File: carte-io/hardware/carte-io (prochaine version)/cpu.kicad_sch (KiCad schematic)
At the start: 24 parts, among them J3 FTSH-105-01-L-DV-007, SW1 SW_Push, SW2 SW_Push, U1 STM32U545VETx, X1 ASE-16.000MHZ-LC-T

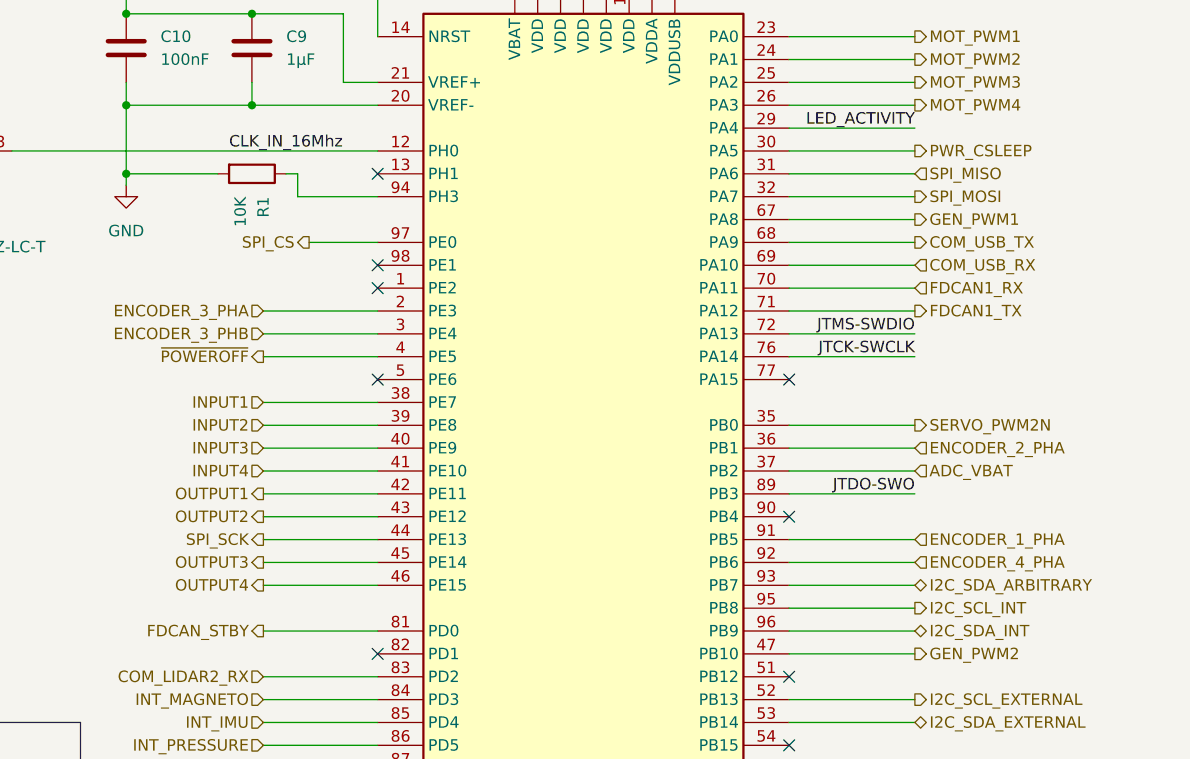
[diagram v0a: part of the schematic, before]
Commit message: Commit de sauvegarde, gros changement sur la carte IO, les connecteurs sont compatibles SeeedStudio Grove. Il faut reprendre une grosse partie du routage et rajouter deux entrées analogiques
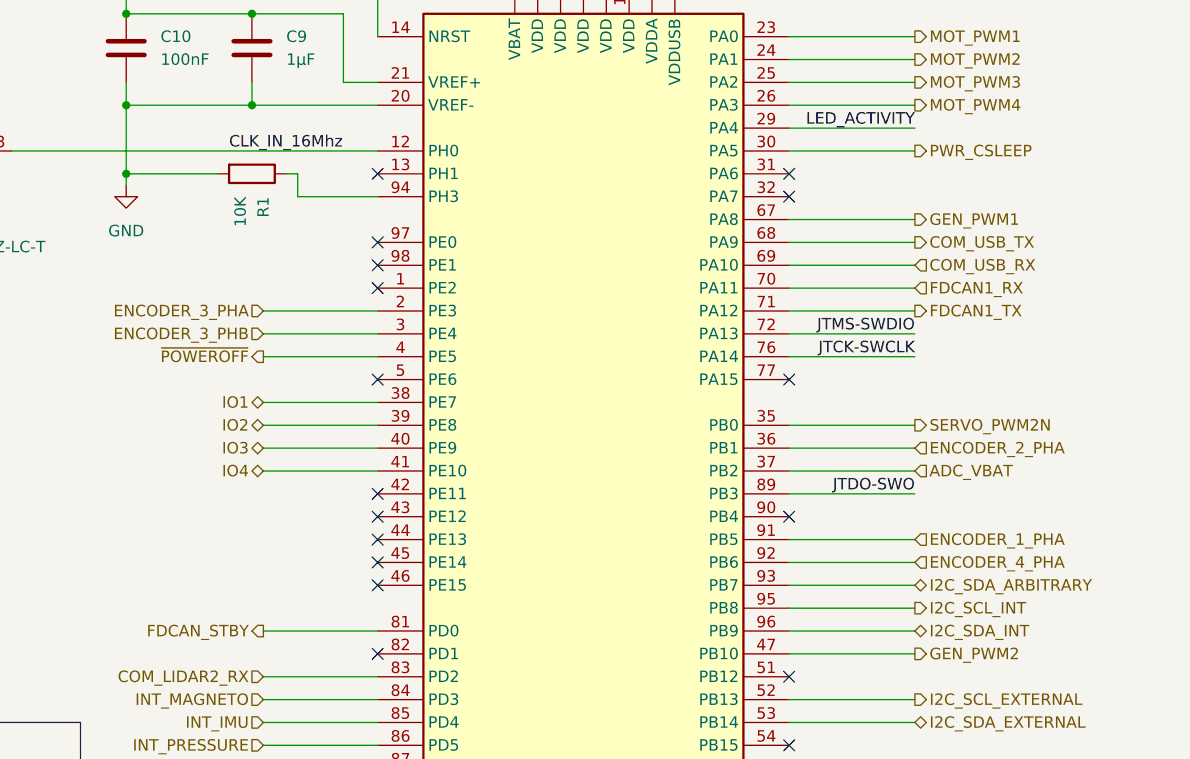
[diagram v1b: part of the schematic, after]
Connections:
- net INPUT1 renamed IO1
- net INPUT2 renamed IO2
- net INPUT3 renamed IO3
- net INPUT4 renamed IO4
- net OUTPUT1: no longer names the net of U1.42 (PE11)
- net OUTPUT2: no longer names the net of U1.43 (PE12)
- net OUTPUT3: no longer names the net of U1.45 (PE14)
- net OUTPUT4: no longer names the net of U1.46 (PE15)
- net SPI_CS: no longer names the net of U1.97 (PE0)
- net SPI_MISO: no longer names the net of U1.31 (PA6)
- net SPI_MOSI: no longer names the net of U1.32 (PA7)
- net SPI_SCK: no longer names the net of U1.44 (PE13)
- no-connect marks 18 -> 26
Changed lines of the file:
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@@
+	)
+	(no_connect
+		(at 104.14 58.42)
+	)
+	(no_connect
+		(at 104.14 86.36)
 	)
 	(no_connect
@@
 	)
 	(no_connect
+		(at 149.86 53.34)
+	)
+	(no_connect
+		(at 104.14 88.9)
+	)
+	(no_connect
+		(at 104.14 91.44)
+	)
+	(no_connect
 		(at 149.86 154.94)
 	)
@@
 	)
 	(no_connect
+		(at 149.86 50.8)
+	)
+	(no_connect
 		(at 104.14 60.96)
 	)
@@
 	)
 	(no_connect
+		(at 104.14 96.52)
+	)
+	(no_connect
 		(at 149.86 157.48)
 	)
@@
 	)
 	(no_connect
+		(at 104.14 93.98)
+	)
+	(no_connect
 		(at 104.14 137.16)
 	)
@@
 	(wire
 		(pts
-			(xy 91.44 91.44) (xy 104.14 91.44)
-		)
-		(stroke
-			(width 0)
-			(type default)
-		)
-	)
-	(wire
-		(pts
 			(xy 50.8 187.96) (xy 58.42 187.96)
 		)
@@
 	(wire
 		(pts
-			(xy 91.44 86.36) (xy 104.14 86.36)
-		)
-		(stroke
-			(width 0)
-			(type default)
-		)
-	)
-	(wire
-		(pts
 			(xy 58.42 187.96) (xy 58.42 189.23)
 		)
@@
 	(wire
 		(pts
-			(xy 91.44 93.98) (xy 104.14 93.98)
-		)
-		(stroke
-			(width 0)
-			(type default)
-		)
-	)
-	(wire
-		(pts
 			(xy 149.86 109.22) (xy 163.83 109.22)
 		)
@@
 	(wire
 		(pts
-			(xy 91.44 88.9) (xy 104.14 88.9)
-		)
-		(stroke
-			(width 0)
-			(type default)
-		)
-	)
-	(wire
-		(pts
 			(xy 25.4 130.81) (xy 25.4 128.27)
 		)
@@
 	(wire
 		(pts
-			(xy 149.86 50.8) (xy 163.83 50.8)
-		)
-		(stroke
-			(width 0)
-			(type default)
-		)
-	)
-	(wire
-		(pts
-			(xy 91.44 96.52) (xy 104.14 96.52)
-		)
-		(stroke
-			(width 0)
-			(type default)
-		)
-	)
-	(wire
-		(pts
 			(xy 76.2 43.18) (xy 90.17 43.18)
 		)
@@
 	(wire
 		(pts
-			(xy 96.52 58.42) (xy 104.14 58.42)
-		)
-		(stroke
-			(width 0)
-			(type default)
-		)
-	)
-	(wire
-		(pts
 			(xy 149.86 71.12) (xy 163.83 71.12)
 		)
@@
 		(pts
 			(xy 127 25.4) (xy 129.54 25.4)
-		)
-		(stroke
-			(width 0)
-			(type default)
-		)
-	)
-	(wire
-		(pts
-			(xy 149.86 53.34) (xy 163.83 53.34)
 		)
 		(stroke
@@
 		)
 	)
-	(hierarchical_label "OUTPUT2"
-		(shape output)
-		(at 91.44 88.9 180)
-		(effects
-			(font
-				(size 1.27 1.27)
-			)
-			(justify right)
-		)
-	)
 	(hierarchical_label "GEN_PWM1"
 		(shape output)
@@
 		)
 	)
-	(hierarchical_label "OUTPUT3"
-		(shape output)
-		(at 91.44 93.98 180)
-		(effects
-			(font
-				(size 1.27 1.27)
-			)
-			(justify right)
-		)
-	)
 	(hierarchical_label "COM_USB_RX"
 		(shape input)
@@
 		)
 	)
-	(hierarchical_label "SPI_SCK"
-		(shape output)
-		(at 91.44 91.44 180)
-		(effects
-			(font
-				(size 1.27 1.27)
-			)
-			(justify right)
-		)
-	)
-	(hierarchical_label "SPI_MOSI"
-		(shape output)
-		(at 163.83 53.34 0)
-		(effects
-			(font
-				(size 1.27 1.27)
-			)
-			(justify left)
-		)
-	)
-	(hierarchical_label "OUTPUT1"
-		(shape output)
-		(at 91.44 86.36 180)
-		(effects
-			(font
-				(size 1.27 1.27)
-			)
-			(justify right)
-		)
-	)
 	(hierarchical_label "GEN_PWM2"
 		(shape output)
@@
 		)
 	)
-	(hierarchical_label "INPUT3"
-		(shape input)
+	(hierarchical_label "IO3"
+		(shape bidirectional)
 		(at 91.44 81.28 180)
 		(effects
@@
 		)
 	)
-	(hierarchical_label "OUTPUT4"
-		(shape output)
-		(at 91.44 96.52 180)
-		(effects
-			(font
-				(size 1.27 1.27)
-			)
-			(justify right)
-		)
-	)
 	(hierarchical_label "ENCODER_2_PHB"
 		(shape input)
@@
 		)
 	)
-	(hierarchical_label "INPUT4"
-		(shape input)
+	(hierarchical_label "IO4"
+		(shape bidirectional)
 		(at 91.44 83.82 180)
 		(effects
@@
 		)
 	)
-	(hierarchical_label "INPUT2"
-		(shape input)
+	(hierarchical_label "IO2"
+		(shape bidirectional)
 		(at 91.44 78.74 180)
 		(effects
@@
 		)
 	)
-	(hierarchical_label "SPI_CS"
-		(shape output)
-		(at 96.52 58.42 180)
-		(effects
-			(font
-				(size 1.27 1.27)
-			)
-			(justify right)
-		)
-	)
 	(hierarchical_label "ADC_VBAT"
 		(shape input)
@@
 		)
 	)
-	(hierarchical_label "INPUT1"
-		(shape input)
+	(hierarchical_label "IO1"
+		(shape bidirectional)
 		(at 91.44 76.2 180)
 		(effects
@@
 		(effects
 			(font
-				(size 1.27 1.27)
-			)
-			(justify left)
-		)
-	)
-	(hierarchical_label "SPI_MISO"
-		(shape input)
-		(at 163.83 50.8 0)
-		(effects
-			(font

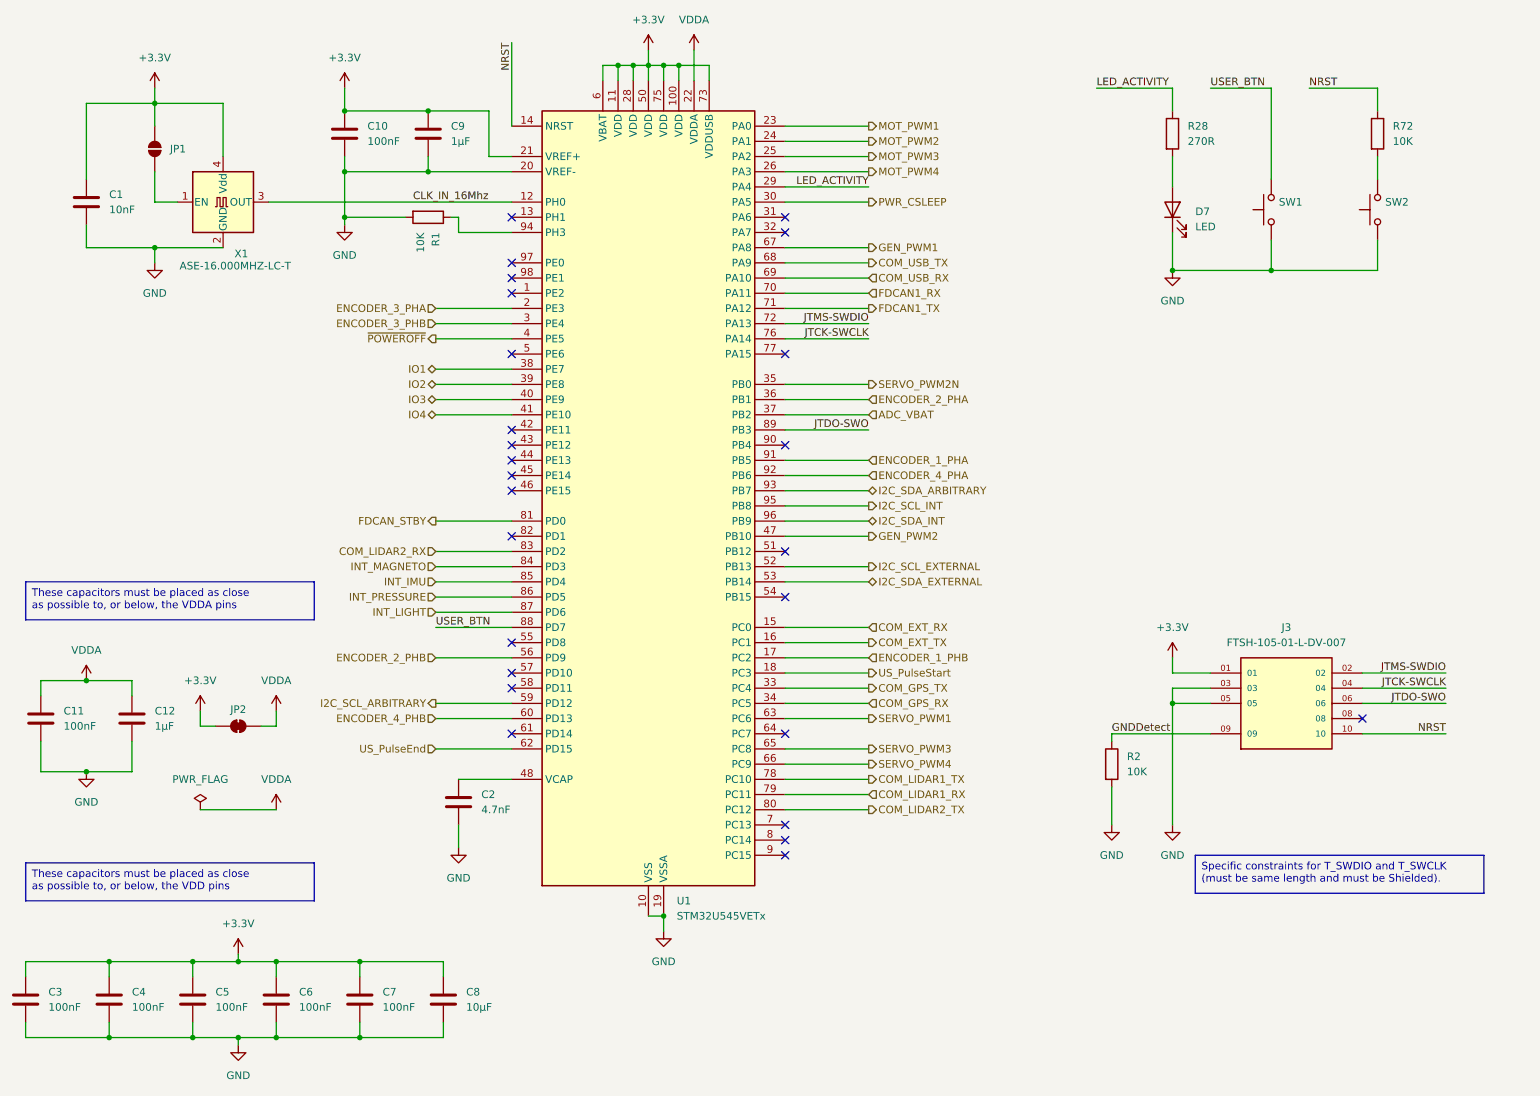
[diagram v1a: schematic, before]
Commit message: -- reorganisation de la carte, - rajout des connecteurs seeedstudio grove - Rajout des deux entrées ADC
travail en cours
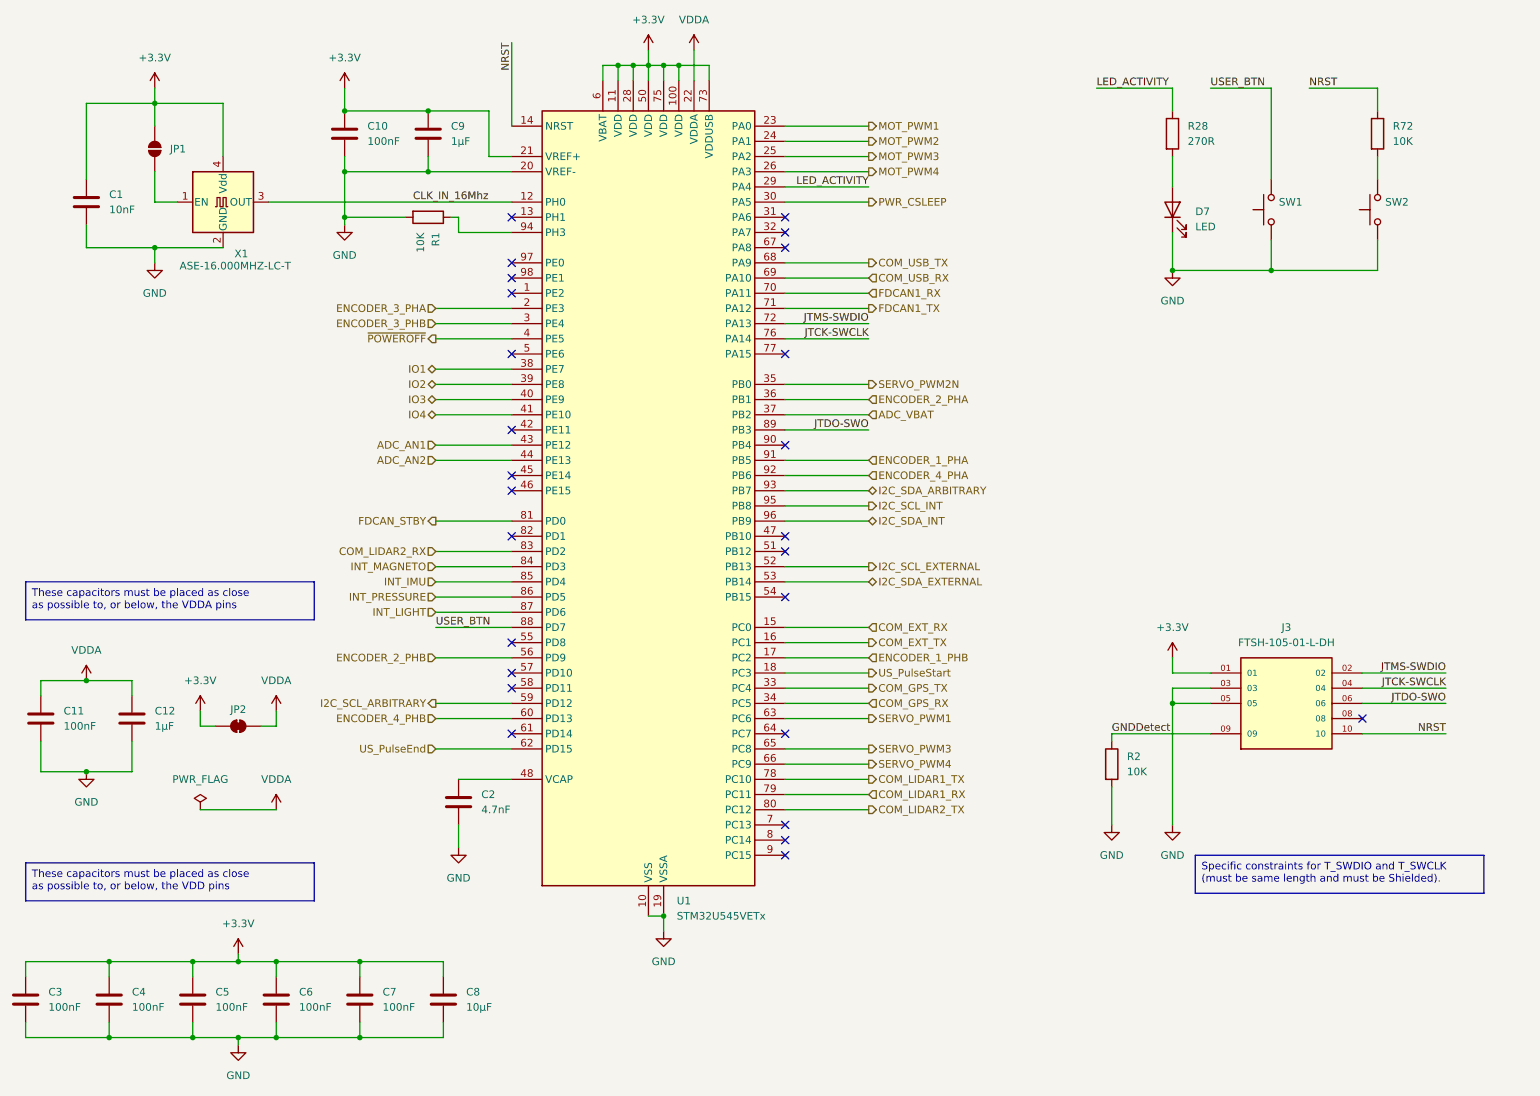
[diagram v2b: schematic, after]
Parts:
- J3: value FTSH-105-01-L-DV-007 -> FTSH-105-01-L-DH; footprint FTSH-105-01-L-DV-007-K:SAMTEC_FTSH-105-X-X-DV-007-P-X -> FTSH-105-01-L-DH:SAMTEC_FTSH-105-01-L-DH
- SW1, SW2: footprint Button_Switch_THT:SW_TH_Tactile_Omron_B3F-10xx -> Button_Switch_SMD:Panasonic_EVQPUJ_EVQPUA
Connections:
- net ADC_AN1: now reaches U1.43 (PE12)
- net ADC_AN2: now reaches U1.44 (PE13)
- net GEN_PWM1: no longer names the net of U1.67 (PA8)
- net GEN_PWM2: no longer names the net of U1.47 (PB10)
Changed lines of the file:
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@@
 	)
 	(no_connect
+		(at 149.86 104.14)
+	)
+	(no_connect
 		(at 104.14 86.36)
 	)
@@
 	)
 	(no_connect
-		(at 104.14 88.9)
-	)
-	(no_connect
-		(at 104.14 91.44)
-	)
-	(no_connect
 		(at 149.86 154.94)
 	)
@@
 	)
 	(no_connect
+		(at 149.86 55.88)
+	)
+	(no_connect
 		(at 149.86 73.66)
 	)
@@
 	(wire
 		(pts
+			(xy 91.44 88.9) (xy 104.14 88.9)
+		)
+		(stroke
+			(width 0)
+			(type default)
+		)
+	)
+	(wire
+		(pts
 			(xy 129.54 25.4) (xy 129.54 27.94)
 		)
@@
 	(wire
 		(pts
-			(xy 149.86 104.14) (xy 163.83 104.14)
-		)
-		(stroke
-			(width 0)
-			(type default)
-		)
-	)
-	(wire
-		(pts
 			(xy 91.44 124.46) (xy 104.14 124.46)
 		)
@@
 	(wire
 		(pts
+			(xy 91.44 91.44) (xy 104.14 91.44)
+		)
+		(stroke
+			(width 0)
+			(type default)
+		)
+	)
+	(wire
+		(pts
 			(xy 149.86 109.22) (xy 163.83 109.22)
 		)
@@
 	(wire
 		(pts
-			(xy 149.86 55.88) (xy 163.83 55.88)
-		)
-		(stroke
-			(width 0)
-			(type default)
-		)
-	)
-	(wire
-		(pts
 			(xy 44.45 55.88) (xy 44.45 58.42)
 		)
@@
 		)
 	)
-	(hierarchical_label "GEN_PWM1"
-		(shape output)
-		(at 163.83 55.88 0)
-		(effects
-			(font
-				(size 1.27 1.27)
-			)
-			(justify left)
-		)
-	)
 	(hierarchical_label "US_PulseStart"
 		(shape output)
@@
 		)
 	)
-	(hierarchical_label "GEN_PWM2"
-		(shape output)
-		(at 163.83 104.14 0)
+	(hierarchical_label "ADC_AN1"
+		(shape input)
+		(at 91.44 88.9 180)
 		(effects
 			(font
 				(size 1.27 1.27)
 			)
-			(justify left)
+			(justify right)
 		)
 	)
@@
 		)
 	)
+	(hierarchical_label "ADC_AN2"
+		(shape input)
+		(at 91.44 91.44 180)
+		(effects
+			(font
+				(size 1.27 1.27)
+			)
+			(justify right)
+		)
+	)
 	(hierarchical_label "COM_USB_TX"
 		(shape output)
@@
 			)
 		)
-		(property "Footprint" "Button_Switch_THT:SW_TH_Tactile_Omron_B3F-10xx"
+		(property "Footprint" "Button_Switch_SMD:Panasonic_EVQPUJ_EVQPUA"
 			(at 243.84 49.53 0)
 			(effects
@@
 			)
 		)
-		(property "Value" "FTSH-105-01-L-DV-007"
+		(property "Value" "FTSH-105-01-L-DH"
 			(at 233.68 121.92 0)
 			(effects
@@
 			)
 		)
-		(property "Footprint" "FTSH-105-01-L-DV-007-K:SAMTEC_FTSH-105-X-X-DV-007-P-X"
+		(property "Footprint" "FTSH-105-01-L-DH:SAMTEC_FTSH-105-01-L-DH"
 			(at 233.68 132.08 0)
 			(effects
@@
 			)
 		)
-		(property "Footprint" "Button_Switch_THT:SW_TH_Tactile_Omron_B3F-10xx"
+		(property "Footprint" "Button_Switch_SMD:Panasonic_EVQPUJ_EVQPUA"
 			(at 226.06 49.53 0)
 			(effects
